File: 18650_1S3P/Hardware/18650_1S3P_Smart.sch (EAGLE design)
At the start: 73 parts, among them J1 CONN_3MICROFIT_RT, J2 GEMS_POWER_PLUGOUTPUT, Q1 MOSFET-NCH-AON7522E, Q2 MOSFET-NCH-AON7522E, Q3 MOSFET-NCH-AON7522E, Q4 MOSFET-NCH-AON7522E, Q5 MOSFET-NCH-AON7522E, Q6 MOSFET-NCH-AON7522E, Q7 MOSFET_PCH-DMP2008, Q8 MOSFET_PCH-DMP2008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

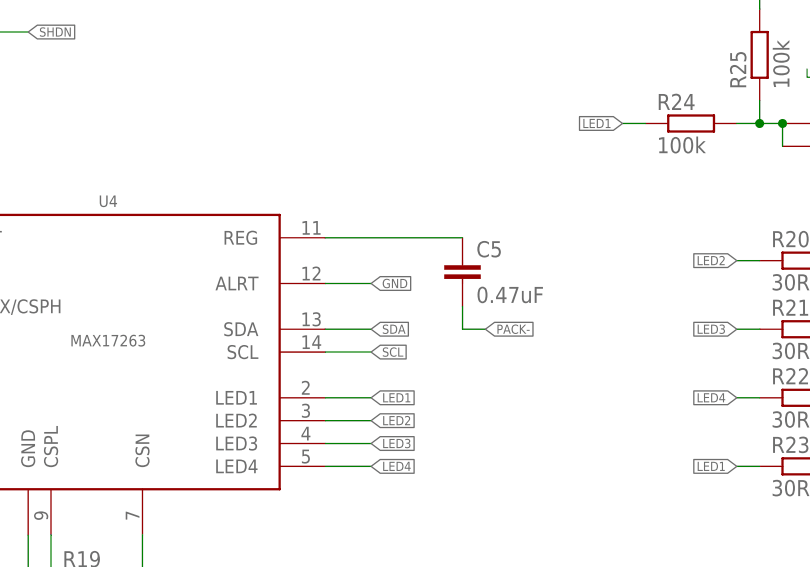
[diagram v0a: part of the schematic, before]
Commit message: Continued layout of 1S3P Smart
Continued layout, connections made, labeling and cleanup required. Made fix to `ALERT` pin connection (had connected to `GND` erroneously vs `PACK-`)
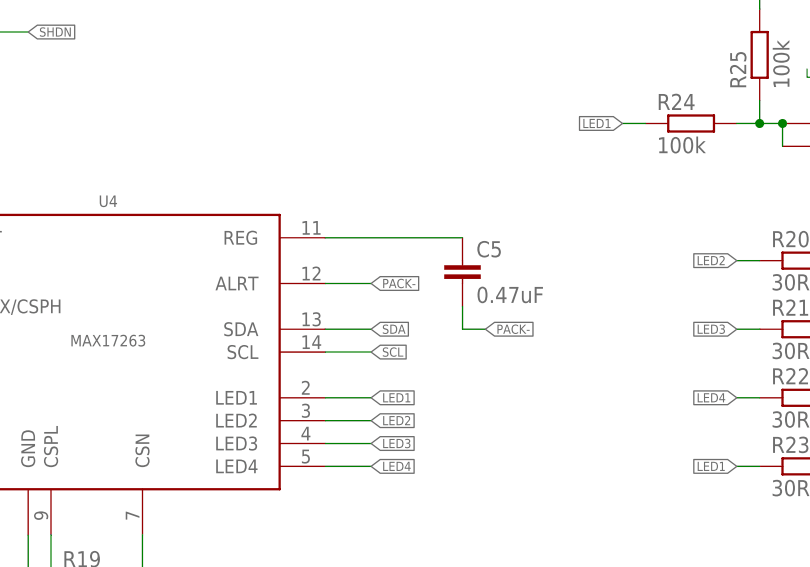
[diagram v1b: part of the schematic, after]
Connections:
- removed net GND: U4.ALRT
- net PACK-: now also U4.ALRT
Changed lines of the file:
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@@
 <label x="241.3" y="83.82" size="1.016" layer="95" rot="R180" xref="yes"/>
+</segment>
+<segment>
+<pinref part="U4" gate="G$1" pin="ALRT"/>
+<wire x1="287.02" y1="167.64" x2="292.1" y2="167.64" width="0.1524" layer="91"/>
+<label x="292.1" y="167.64" size="1.016" layer="95" xref="yes"/>
 </segment>
 </net>
@@
 </segment>
 </net>
-<net name="GND" class="0">
-<segment>
-<pinref part="U4" gate="G$1" pin="ALRT"/>
-<wire x1="287.02" y1="167.64" x2="292.1" y2="167.64" width="0.1524" layer="91"/>
-<label x="292.1" y="167.64" size="1.016" layer="95" xref="yes"/>
-</segment>
-</net>

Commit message: Layout and ref designator cleanup, ready for final verification
Continued layout cleanup, layout should be final barring final verification
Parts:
- BT1, BT2, BT3: value 186501042P -> 186501042P_NOSILK; device bschulz:186501042P -> bschulz:186501042P_NOSILK
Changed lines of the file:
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@@
 <part name="Q1" library="bschulz" deviceset="MOSFET-NCH" device="-AON7522E"/>
 <part name="Q2" library="bschulz" deviceset="MOSFET-NCH" device="-AON7522E"/>
-<part name="BT1" library="bschulz" deviceset="18650" device="1042P"/>
+<part name="BT1" library="bschulz" deviceset="18650" device="1042P_NOSILK" value="186501042P_NOSILK"/>
 <part name="D1" library="bschulz" deviceset="DIODE_SCHOTTKY" device="SOD-323">
 <attribute name="DIGIKEY" value="BAT54WS-FDICT-ND"/>
@@
 <part name="Q3" library="bschulz" deviceset="MOSFET-NCH" device="-AON7522E"/>
 <part name="Q4" library="bschulz" deviceset="MOSFET-NCH" device="-AON7522E"/>
-<part name="BT2" library="bschulz" deviceset="18650" device="1042P"/>
+<part name="BT2" library="bschulz" deviceset="18650" device="1042P_NOSILK" value="186501042P_NOSILK"/>
 <part name="D2" library="bschulz" deviceset="DIODE_SCHOTTKY" device="SOD-323">
 <attribute name="DIGIKEY" value="BAT54WS-FDICT-ND"/>
@@
 <part name="Q5" library="bschulz" deviceset="MOSFET-NCH" device="-AON7522E"/>
 <part name="Q6" library="bschulz" deviceset="MOSFET-NCH" device="-AON7522E"/>
-<part name="BT3" library="bschulz" deviceset="18650" device="1042P"/>
+<part name="BT3" library="bschulz" deviceset="18650" device="1042P_NOSILK" value="186501042P_NOSILK"/>
 <part name="D3" library="bschulz" deviceset="DIODE_SCHOTTKY" device="SOD-323">
 <attribute name="DIGIKEY" value="BAT54WS-FDICT-ND"/>
